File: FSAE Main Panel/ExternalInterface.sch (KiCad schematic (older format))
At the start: 17 parts, among them J201 Conn_01x06, J202 Cortex_Debug, J203 Conn_01x04, J204 TE_84953-6_FPC, SW1 B3W-1020, SW2 B3W-1020

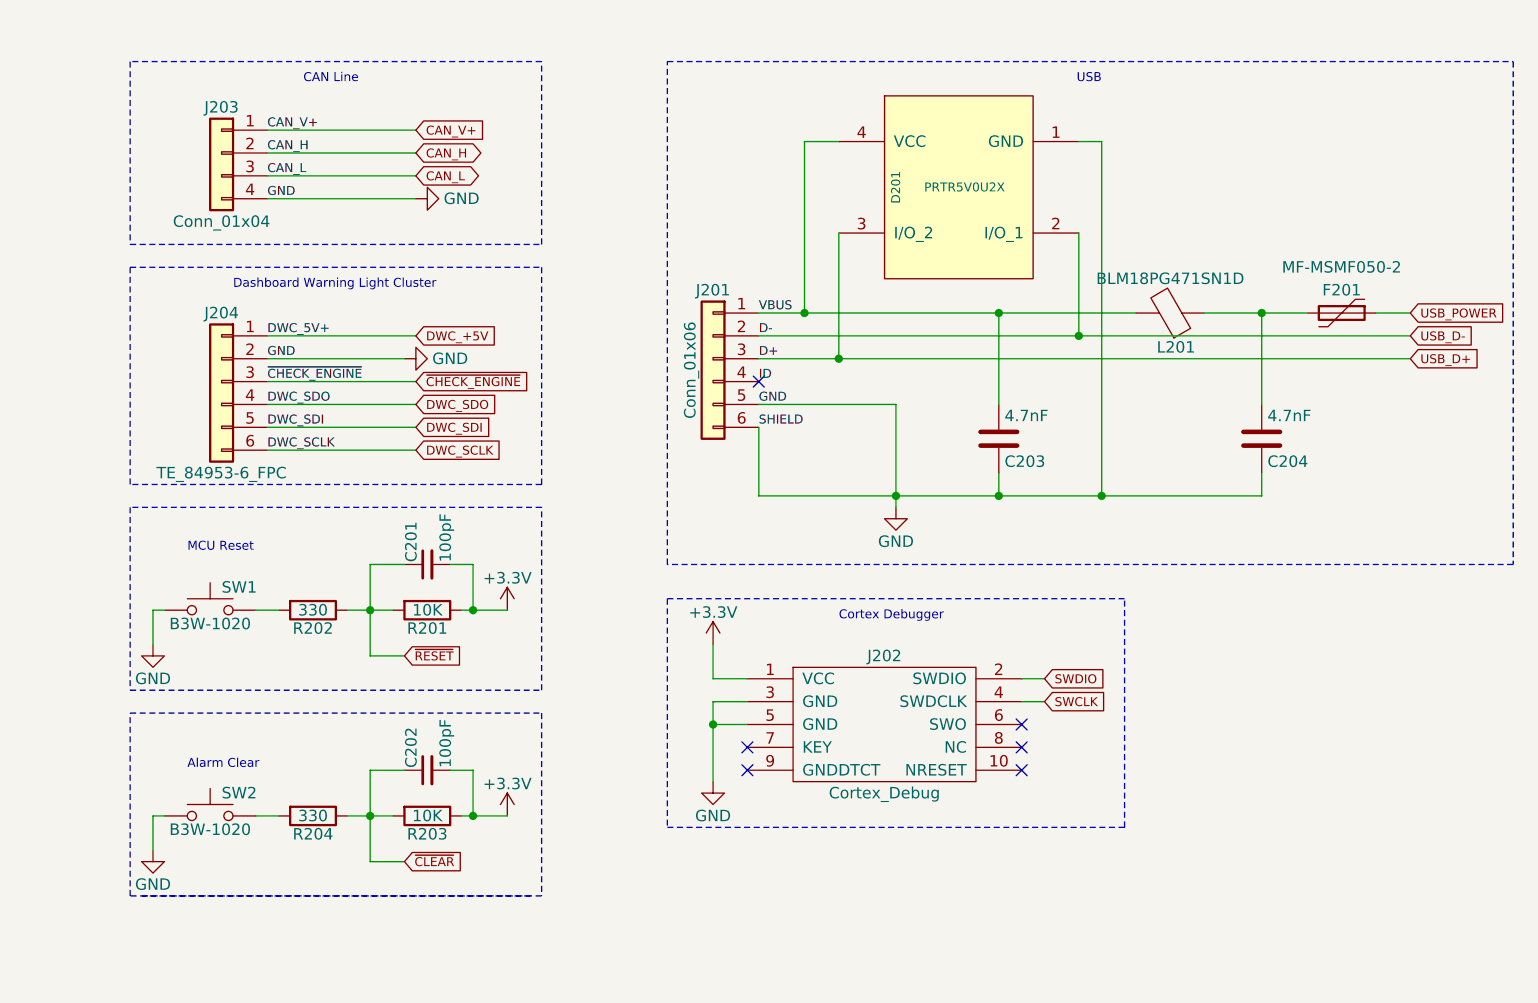
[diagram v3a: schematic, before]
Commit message: Updated Footprint Association
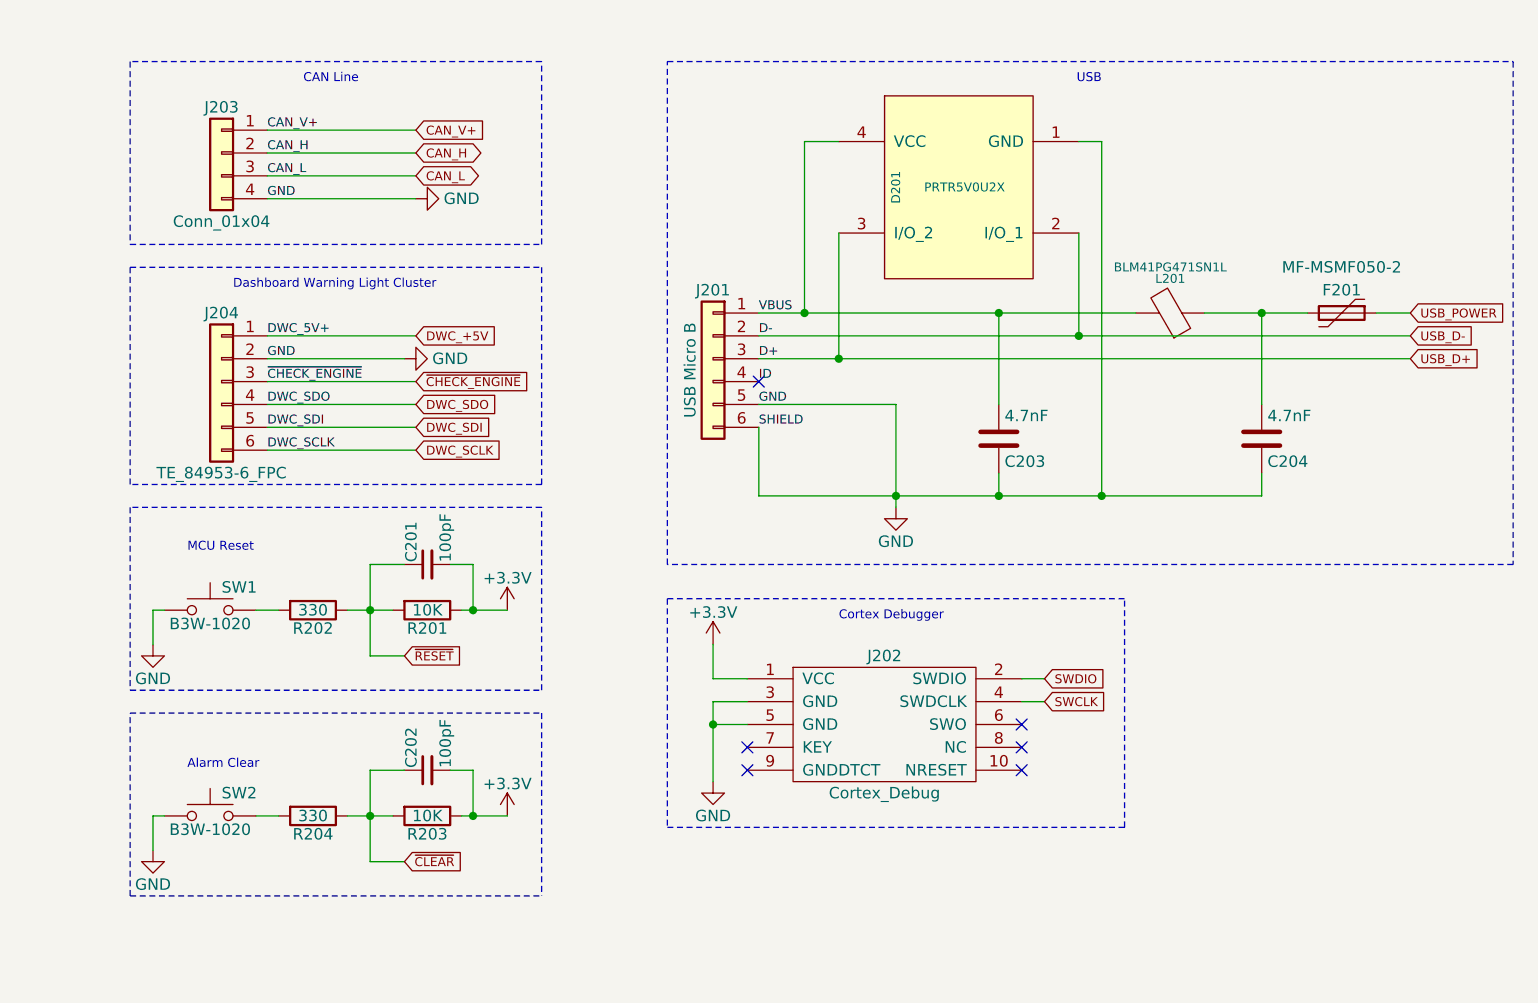
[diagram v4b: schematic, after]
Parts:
- C201, C202: footprint (none) -> Capacitors_SMD:C_0805; Description (none) -> Ceramic 100pF 10V X7R 0805
- C203, C204: footprint (none) -> Capacitors_SMD:C_1206; Description (none) -> Ceramic 4700pF 10V X7R 1206
- D201: footprint (none) -> TO_SOT_Packages_SMD:SOT-143; Description (none) -> ESD Protection Diode
- F201: Description (none) -> 500mA Resettable Fuse 1812
- J201: value Conn_01x06 -> USB Micro B
- L201: value BLM18PG471SN1D -> BLM41PG471SN1L; Description (none) -> 470 Ohm Ferrite Bead 1806
- R201, R202, R203, R204: footprint (none) -> Resistors_SMD:R_1206
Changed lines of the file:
@@
 CAN_V+
 $Comp
-L power:GND #PWR204
+L power:GND #PWR0204
 U 1 1 5BE24FFA
 P 1900 1450
-F 0 "#PWR204" H 1900 1200 50  0001 C CNN
+F 0 "#PWR0204" H 1900 1200 50  0001 C CNN
 F 1 "GND" V 1900 1250 50  0000 C CNN
 F 2 "" H 1900 1450 50  0001 C CNN
@@
 DWC_+5V
 $Comp
-L power:GND #PWR203
+L power:GND #PWR0203
 U 1 1 5BE9B884
 P 1850 2150
-F 0 "#PWR203" H 1850 1900 50  0001 C CNN
+F 0 "#PWR0203" H 1850 1900 50  0001 C CNN
 F 1 "GND" V 1850 1950 50  0000 C CNN
 F 2 "" H 1850 2150 50  0001 C CNN
@@
 Alarm Clear
 $Comp
-L power:GND #PWR201
+L power:GND #PWR0201
 U 1 1 5BE9BAFE
 P 750 3400
-F 0 "#PWR201" H 750 3150 50  0001 C CNN
+F 0 "#PWR0201" H 750 3150 50  0001 C CNN
 F 1 "GND" H 750 3250 50  0000 C CNN
 F 2 "" H 750 3400 50  0001 C CNN
@@
 $EndComp
 $Comp
-L power:GND #PWR202
+L power:GND #PWR0202
 U 1 1 5BE9BB22
 P 750 4300
-F 0 "#PWR202" H 750 4050 50  0001 C CNN
+F 0 "#PWR0202" H 750 4050 50  0001 C CNN
 F 1 "GND" H 750 4150 50  0000 C CNN
 F 2 "" H 750 4300 50  0001 C CNN
@@
 F 0 "R201" V 2030 3250 50  0000 C CNN
 F 1 "10K" V 1950 3250 50  0000 C CNN
-F 2 "" V 1880 3250 50  0001 C CNN
+F 2 "Resistors_SMD:R_1206" V 1880 3250 50  0001 C CNN
 F 3 "" H 1950 3250 50  0001 C CNN
 	1    1950 3250
@@
 F 0 "C201" H 1960 3120 50  0000 L CNN
 F 1 "100pF" H 1960 2970 50  0000 L CNN
-F 2 "" H 1950 3050 50  0001 C CNN
+F 2 "Capacitors_SMD:C_0805" H 1950 3050 50  0001 C CNN
 F 3 "" H 1950 3050 50  0001 C CNN
+F 4 "Ceramic 100pF 10V X7R 0805" H 1950 3050 50  0001 C CNN "Description"
 	1    1950 3050
 	0    -1   -1   0
@@
 F 0 "R202" V 1530 3250 50  0000 C CNN
 F 1 "330" V 1450 3250 50  0000 C CNN
-F 2 "" V 1380 3250 50  0001 C CNN
+F 2 "Resistors_SMD:R_1206" V 1380 3250 50  0001 C CNN
 F 3 "" H 1450 3250 50  0001 C CNN
 	1    1450 3250
@@
 F 0 "R203" V 2030 4150 50  0000 C CNN
 F 1 "10K" V 1950 4150 50  0000 C CNN
-F 2 "" V 1880 4150 50  0001 C CNN
+F 2 "Resistors_SMD:R_1206" V 1880 4150 50  0001 C CNN
 F 3 "" H 1950 4150 50  0001 C CNN
 	1    1950 4150
@@
 F 0 "C202" H 1960 4020 50  0000 L CNN
 F 1 "100pF" H 1960 3870 50  0000 L CNN
-F 2 "" H 1950 3950 50  0001 C CNN
+F 2 "Capacitors_SMD:C_0805" H 1950 3950 50  0001 C CNN
 F 3 "" H 1950 3950 50  0001 C CNN
+F 4 "Ceramic 100pF 10V X7R 0805" H 1950 3950 50  0001 C CNN "Description"
 	1    1950 3950
 	0    -1   -1   0
@@
 F 0 "R204" V 1530 4150 50  0000 C CNN
 F 1 "330" V 1450 4150 50  0000 C CNN
-F 2 "" V 1380 4150 50  0001 C CNN
+F 2 "Resistors_SMD:R_1206" V 1380 4150 50  0001 C CNN
 F 3 "" H 1450 4150 50  0001 C CNN
 	1    1450 4150
@@
 $EndComp
 $Comp
-L power:+3.3V #PWR205
+L power:+3.3V #PWR0205
 U 1 1 5BE9CCF2
 P 2300 3250
-F 0 "#PWR205" H 2300 3100 50  0001 C CNN
+F 0 "#PWR0205" H 2300 3100 50  0001 C CNN
 F 1 "+3.3V" H 2300 3390 50  0000 C CNN
 F 2 "" H 2300 3250 50  0001 C CNN
@@
 $EndComp
 $Comp
-L power:+3.3V #PWR206
+L power:+3.3V #PWR0206
 U 1 1 5BE9CD22
 P 2300 4150
-F 0 "#PWR206" H 2300 4000 50  0001 C CNN
+F 0 "#PWR0206" H 2300 4000 50  0001 C CNN
 F 1 "+3.3V" H 2300 4290 50  0000 C CNN
 F 2 "" H 2300 4150 50  0001 C CNN
@@
 P 3200 2150
 F 0 "J201" H 3200 2450 50  0000 C CNN
-F 1 "Conn_01x06" V 3300 2100 50  0000 C CNN
+F 1 "USB Micro B" V 3300 2100 50  0000 C CNN
 F 2 "" H 3200 2150 50  0001 C CNN
 F 3 "" H 3200 2150 50  0001 C CNN
@@
 $EndComp
 $Comp
-L power:GND #PWR209
+L power:GND #PWR0209
 U 1 1 5BF06480
 P 4000 2800
-F 0 "#PWR209" H 4000 2550 50  0001 C CNN
+F 0 "#PWR0209" H 4000 2550 50  0001 C CNN
 F 1 "GND" H 4000 2650 50  0000 C CNN
 F 2 "" H 4000 2800 50  0001 C CNN
@@
 U 1 1 5BF06486
 P 5200 1950
-F 0 "L201" V 5050 1975 50  0000 C CNN
-F 1 "BLM18PG471SN1D" V 5350 1950 50  0000 C CNN
+F 0 "L201" V 5350 1950 39  0000 C CNN
+F 1 "BLM41PG471SN1L" V 5400 1950 39  0000 C CNN
 F 2 "" V 5130 1950 50  0001 C CNN
 F 3 "" H 5200 1950 50  0001 C CNN
+F 4 "470 Ohm Ferrite Bead 1806" V 5200 1950 50  0001 C CNN "Description"
 	1    5200 1950
 	0    1    -1   0
@@
 F 0 "C203" H 4475 2600 50  0000 L CNN
 F 1 "4.7nF" H 4475 2400 50  0000 L CNN
-F 2 "" H 4488 2350 50  0001 C CNN
+F 2 "Capacitors_SMD:C_1206" H 4488 2350 50  0001 C CNN
 F 3 "" H 4450 2500 50  0001 C CNN
+F 4 "Ceramic 4700pF 10V X7R 1206" H 4450 2500 50  0001 C CNN "Description"
 	1    4450 2500
 	1    0    0    1
@@
 F 0 "D201" H 4300 1700 39  0000 C CNN
 F 1 "PRTR5V0U2X" V 4300 1400 39  0000 C CNN
-F 2 "" H 4300 1400 60  0001 C CNN
+F 2 "TO_SOT_Packages_SMD:SOT-143" H 4300 1400 60  0001 C CNN
 F 3 "" H 4300 1400 60  0001 C CNN
+F 4 "ESD Protection Diode" H 4300 1400 50  0001 C CNN "Description"
 	1    4300 1400
 	0    -1   1    0
@@
 F 0 "C204" H 5625 2600 50  0000 L CNN
 F 1 "4.7nF" H 5625 2400 50  0000 L CNN
-F 2 "" H 5638 2350 50  0001 C CNN
+F 2 "Capacitors_SMD:C_1206" H 5638 2350 50  0001 C CNN
 F 3 "" H 5600 2500 50  0001 C CNN
+F 4 "Ceramic 4700pF 10V X7R 1206" H 5600 2500 50  0001 C CNN "Description"
 	1    5600 2500
 	1    0    0    1
@@
 	750  3250 750  3400
 Wire Wire Line
-	1600 3250 1800 3250
-Wire Wire Line
-	2100 3250 2300 3250
-Wire Wire Line
-	1700 3050 1700 3450
+	1600 3250 1700 3250
+Wire Wire Line
+	2100 3250 2150 3250
+Wire Wire Line
+	1700 3050 1700 3250
 Connection ~ 1700 3250
 Wire Notes Line
@@
 Wire Notes Line
 	2450 3700 2450 4500
-Wire Notes Line
-	2400 4500 650  4500
 Wire Notes Line
 	650  4500 650  3700
@@
 Connection ~ 2150 3250
 Wire Wire Line
-	1600 4150 1800 4150
-Wire Wire Line
-	2100 4150 2300 4150
-Wire Wire Line
-	1700 3950 1700 4350
+	1600 4150 1700 4150
+Wire Wire Line
+	2100 4150 2150 4150
+Wire Wire Line
+	1700 3950 1700 4150
 Connection ~ 1700 4150
-Wire Notes Line
-	2450 4500 700  4500
 Wire Wire Line
 	1200 4150 1300 4150
@@
 Connection ~ 2150 4150
 Wire Wire Line
-	3400 1950 5050 1950
+	3400 1950 3600 1950
 Wire Wire Line
 	3400 2350 4000 2350
 Wire Wire Line
-	4000 2350 4000 2800
-Wire Wire Line
-	3400 2050 6250 2050
+	4000 2350 4000 2750
+Wire Wire Line
+	3400 2050 4800 2050
 Wire Wire Line
 	3750 1600 3750 2150
 Connection ~ 3750 2150
 Wire Wire Line
-	3400 2150 6250 2150
+	3400 2150 3750 2150
 Wire Wire Line
 	3750 1200 3600 1200
@@
 	5600 2750 5600 2650
 Wire Wire Line
-	3400 2750 5600 2750
+	3400 2750 4000 2750
 Connection ~ 4000 2750
 Connection ~ 4900 2750
@@
 F 2 "" H 6000 1750 50  0001 L CNN
 F 3 "" H 5950 1950 50  0001 C CNN
+F 4 "500mA Resettable Fuse 1812" V 5950 1950 50  0001 C CNN "Description"
 	1    5950 1950
 	0    1    1    0
 $EndComp
 Wire Wire Line
-	5350 1950 5800 1950
+	5350 1950 5600 1950
 Wire Wire Line
 	6100 1950 6250 1950
@@
 $EndComp
 $Comp
-L power:+3.3V #PWR207
+L power:+3.3V #PWR0207
 U 1 1 5BFE98A3
 P 3200 3400
-F 0 "#PWR207" H 3200 3250 50  0001 C CNN
+F 0 "#PWR0207" H 3200 3250 50  0001 C CNN
 F 1 "+3.3V" H 3200 3540 50  0000 C CNN
 F 2 "" H 3200 3400 50  0001 C CNN
@@
 $EndComp
 $Comp
-L power:GND #PWR208
+L power:GND #PWR0208
 U 1 1 5BFE993E
 P 3200 4000
-F 0 "#PWR208" H 3200 3750 50  0001 C CNN
+F 0 "#PWR0208" H 3200 3750 50  0001 C CNN
 F 1 "GND" H 3200 3850 50  0000 C CNN
 F 2 "" H 3200 4000 50  0001 C CNN
@@
 	3350 3650 3200 3650
 Wire Wire Line
-	3200 3650 3200 4000
+	3200 3650 3200 3750
 Wire Wire Line
 	3350 3750 3200 3750
@@
 NoConn ~ 3350 3850
 NoConn ~ 3350 3950
+Wire Wire Line
+	1700 3250 1800 3250
+Wire Wire Line
+	1700 3250 1700 3450
+Wire Wire Line
+	2150 3250 2300 3250
+Wire Wire Line
+	1700 4150 1800 4150
+Wire Wire Line
+	1700 4150 1700 4350
+Wire Wire Line
+	2150 4150 2300 4150
+Wire Wire Line
+	3750 2150 6250 2150
+Wire Wire Line
+	3600 1950 4450 1950
+Wire Wire Line
+	4450 1950 5050 1950
+Wire Wire Line
+	5600 1950 5800 1950
+Wire Wire Line
+	4800 2050 6250 2050
+Wire Wire Line
+	4000 2750 4000 2800
+Wire Wire Line
+	4000 2750 4450 2750
+Wire Wire Line
+	4900 2750 5600 2750
+Wire Wire Line
+	4450 2750 4900 2750
+Wire Wire Line
+	3200 3750 3200 4000
+Wire Notes Line
+	650  4500 2450 4500
 $EndSCHEMATC

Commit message: New footprints, finished associating footprints
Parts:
- F201: footprint (none) -> MF-MSMF050-2:MF-MSMF050-2
- J201: footprint (none) -> 10118192-0001LF:10118192-0001LF
- J202: footprint (none) -> Pin_Headers:Pin_Header_Straight_2x05_Pitch1.27mm
- J203: footprint (none) -> Connectors_JST:JST_VH_B4PS-VH_2x4x3.96mm_Horizontal
- L201: footprint (none) -> Inductors_SMD:L_1806
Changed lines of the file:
@@
 F 0 "J203" H 1050 1450 50  0000 C CNN
 F 1 "Conn_01x04" H 1050 950 50  0000 C CNN
-F 2 "" H 1050 1250 50  0001 C CNN
+F 2 "Connectors_JST:JST_VH_B4PS-VH_2x4x3.96mm_Horizontal" H 1050 1250 50  0001 C CNN
 F 3 "" H 1050 1250 50  0001 C CNN
 	1    1050 1250
@@
 F 0 "J201" H 3200 2450 50  0000 C CNN
 F 1 "USB Micro B" V 3300 2100 50  0000 C CNN
-F 2 "" H 3200 2150 50  0001 C CNN
+F 2 "10118192-0001LF:10118192-0001LF" H 3200 2150 50  0001 C CNN
 F 3 "" H 3200 2150 50  0001 C CNN
 	1    3200 2150
@@
 F 0 "L201" V 5350 1950 39  0000 C CNN
 F 1 "BLM41PG471SN1L" V 5400 1950 39  0000 C CNN
-F 2 "" V 5130 1950 50  0001 C CNN
+F 2 "Inductors_SMD:L_1806" V 5130 1950 50  0001 C CNN
 F 3 "" H 5200 1950 50  0001 C CNN
 F 4 "470 Ohm Ferrite Bead 1806" V 5200 1950 50  0001 C CNN "Description"
@@
 F 0 "F201" V 5850 1950 50  0000 C CNN
 F 1 "MF-MSMF050-2" V 5750 1950 50  0000 C CNN
-F 2 "" H 6000 1750 50  0001 L CNN
+F 2 "MF-MSMF050-2:MF-MSMF050-2" H 6000 1750 50  0001 L CNN
 F 3 "" H 5950 1950 50  0001 C CNN
 F 4 "500mA Resettable Fuse 1812" V 5950 1950 50  0001 C CNN "Description"
@@
 F 0 "J202" H 3950 4050 50  0000 C CNN
 F 1 "Cortex_Debug" H 3950 3450 50  0000 C CNN
-F 2 "" H 4100 3750 39  0001 C CNN
+F 2 "Pin_Headers:Pin_Header_Straight_2x05_Pitch1.27mm" H 4100 3750 39  0001 C CNN
 F 3 "" H 4100 3750 39  0001 C CNN
 	1    3950 3750
